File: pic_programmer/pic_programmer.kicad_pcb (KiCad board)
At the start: 2 copper layers, 160 x 99.1 mm, 65 parts, among them J1 DB9-FEMAL, P1 CONN_2, P101 CONN_1, P102 CONN_1, P103 CONN_1, P104 CONN_1, P105 CONN_1, P106 CONN_1, P2 SUPP28, P3 SUPP40, P4 CONN_01X03, P5 CONN_01X03, Q1 BC237, Q2 BC307, Q3 BC307, U1 24Cxx, U2 74HC125, U3 7805, U4 LT1373, U5 PIC_18_PINS, U6 PIC_8_PINS

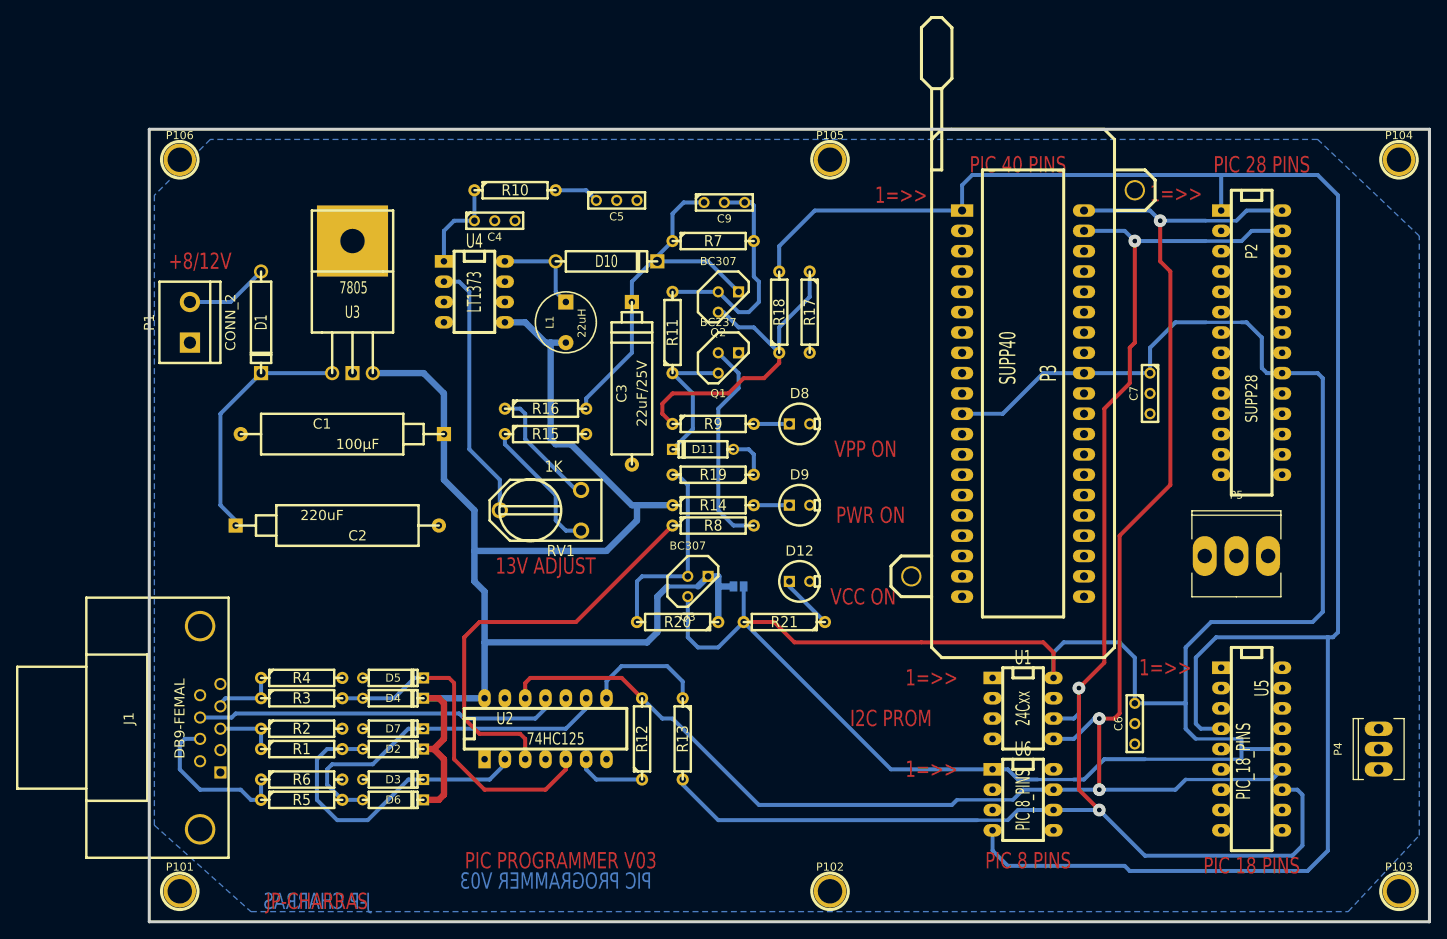
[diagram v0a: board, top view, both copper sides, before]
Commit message: performanced pcb layout with free-router, added one extra track to practice key shortcuts: x, v
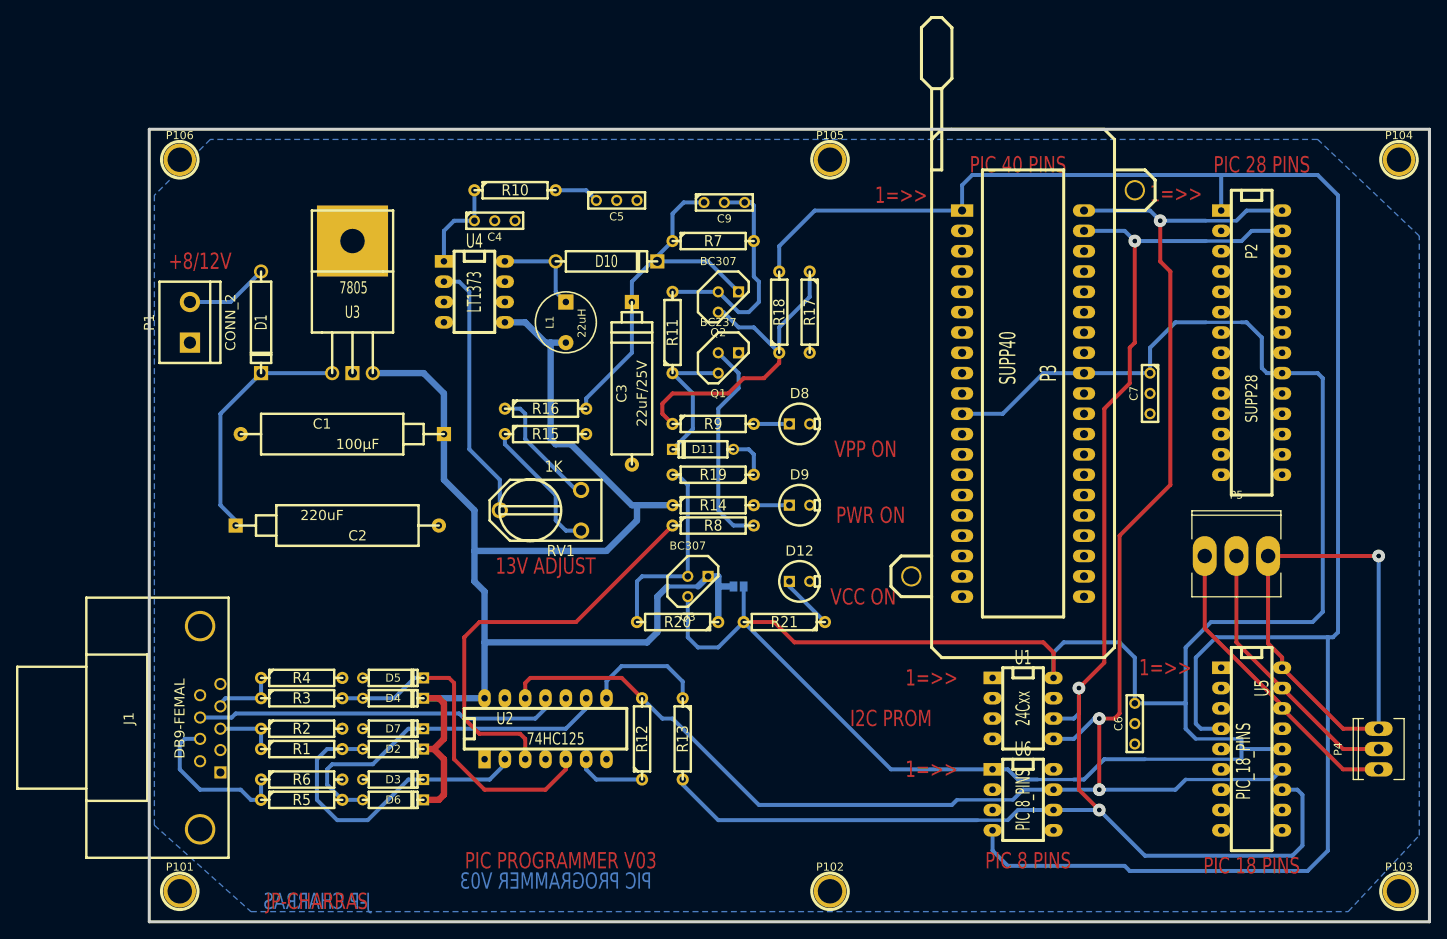
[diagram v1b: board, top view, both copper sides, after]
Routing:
- net /pic_sockets/a1: track 0.00 -> 65.3 mm, vias 0 -> 1
- net /pic_sockets/a3: track 0.00 -> 38.3 mm
- net /pic_sockets/a2: track 0.00 -> 34.1 mm
